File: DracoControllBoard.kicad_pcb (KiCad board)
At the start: 2 copper layers, 96.5 x 61.5 mm, 22 parts, among them SW1 SW_Push, SW10 SW_Push, SW11 SW_Push, SW12 SW_Push, SW2 SW_Push, SW3 SW_Push, SW4 SW_Push, SW5 SW_Push, SW6 SW_Push, SW7 SW_Push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

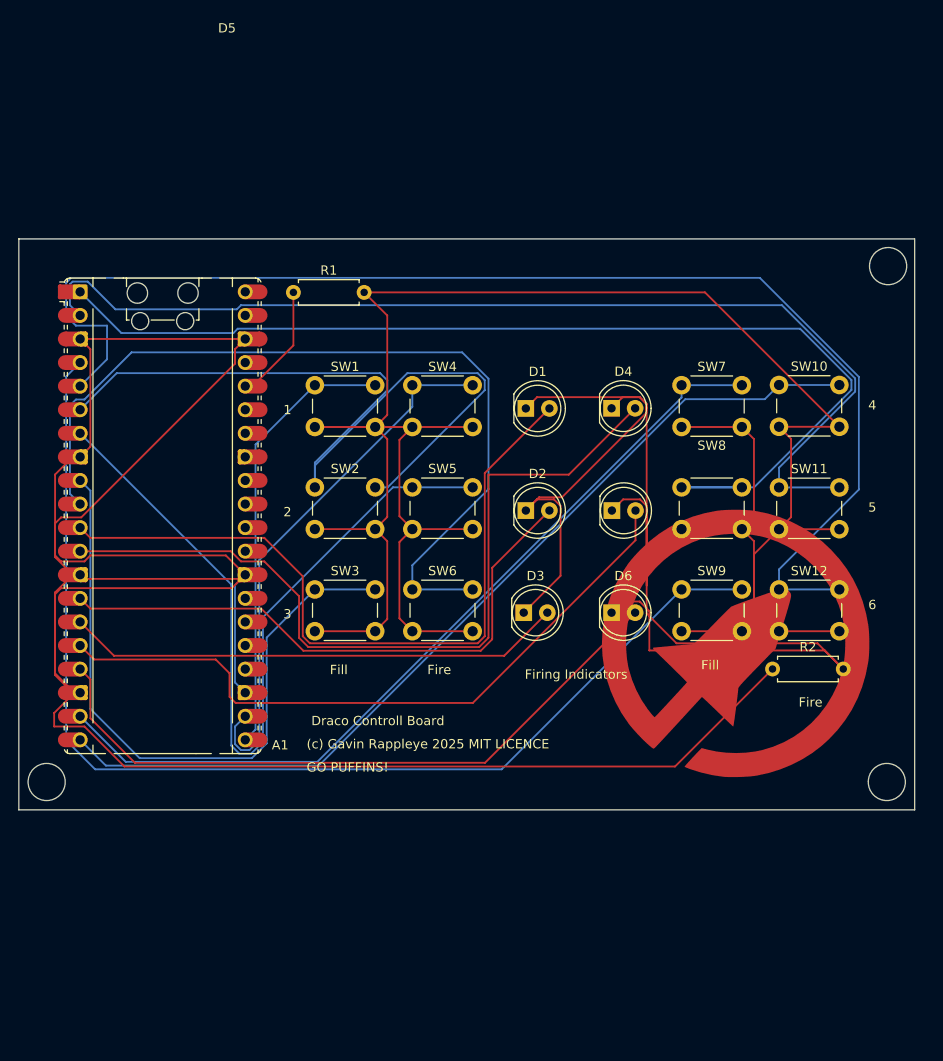
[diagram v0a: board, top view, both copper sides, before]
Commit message: fixted resistor issues
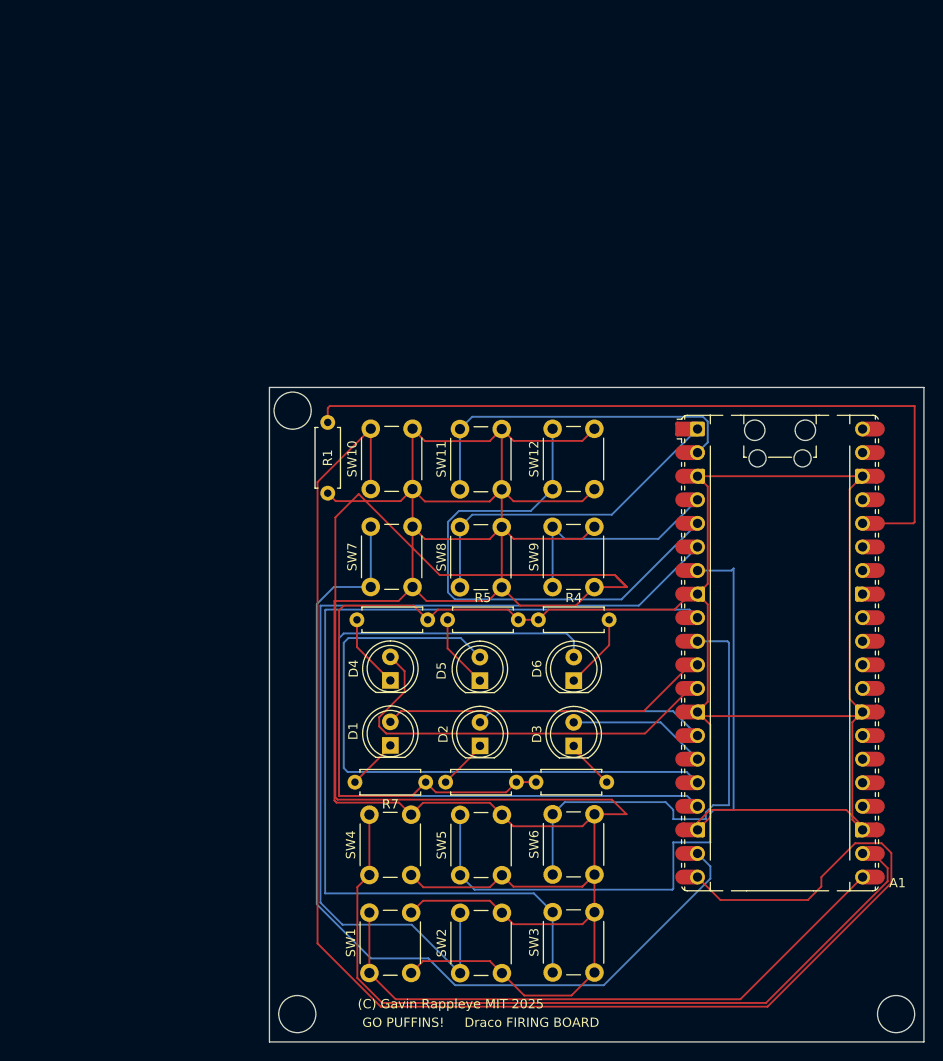
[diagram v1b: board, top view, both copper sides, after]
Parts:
- removed G***: LOGO, LOGO
- added R3: R, Resistor_THT:R_Axial_DIN0207_L6.3mm_D2.5mm_P7.62mm_Horizontal, F.Cu at (54.5, 67.0)
- added R4: R, Resistor_THT:R_Axial_DIN0207_L6.3mm_D2.5mm_P7.62mm_Horizontal, F.Cu at (64.5, 49.5)
- added R5: R, Resistor_THT:R_Axial_DIN0207_L6.3mm_D2.5mm_P7.62mm_Horizontal, F.Cu at (54.7, 49.5)
- added R6: R, Resistor_THT:R_Axial_DIN0207_L6.3mm_D2.5mm_P7.62mm_Horizontal, F.Cu at (52.5, 49.5)
- added R7: R, Resistor_THT:R_Axial_DIN0207_L6.3mm_D2.5mm_P7.62mm_Horizontal, F.Cu at (52.3, 67.0)
- moved A1 68.1 mm to (90.5, 53.1)
- moved SW1 63.6 mm to (46.3, 87.6), turned to 90 degrees
- moved SW2 54.6 mm to (56.0, 87.6), turned to 90 degrees
- moved SW4 53.0 mm to (46.3, 77.0), turned to 90 degrees
- moved SW3 48.6 mm to (66.0, 87.5), turned to 90 degrees
- moved SW10 45.4 mm to (46.4, 35.4), turned to 90 degrees
- moved SW5 42.1 mm to (56.0, 77.0), turned to 90 degrees
- moved SW7 39.9 mm to (46.4, 46.0), turned to 90 degrees
- moved D1 39.1 mm to (48.5, 63.1), turned to 90 degrees
- moved D4 37.8 mm to (48.5, 56.1), turned to 90 degrees
- moved SW11 34.4 mm to (56.0, 35.5), turned to 90 degrees
- moved SW6 34.2 mm to (66.0, 77.0), turned to 90 degrees
- moved R2 28.2 mm to (64.2, 67.0)
- moved SW12 26.7 mm to (66.0, 35.5), turned to 90 degrees
- moved SW8 26.2 mm to (56.0, 46.0), turned to 90 degrees
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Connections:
- D2 pad 1: Net-(D1-K) -> Net-(D2-K)
- D3 pad 1: Net-(D1-K) -> Net-(D3-K)
- D4 pad 1: Net-(D1-K) -> Net-(D4-K)
- D5 pad 1: Net-(D1-K) -> Net-(D5-K)
- D6 pad 1: Net-(D1-K) -> Net-(D6-K)
- R2 pad 2: Net-(D1-K) -> Net-(D3-K)
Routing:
- net Net-(D1-K): track 150.6 -> 5.54 mm
- net Net-(R1-Pad2): track 263.7 -> 387.5 mm
- net Net-(A1-GPIO2): track 123.4 -> 24.4 mm
- net Net-(A1-GPIO3): track 139.1 -> 57.4 mm
- net Net-(A1-GPIO0): track 117.6 -> 36.5 mm
- net Net-(A1-GPIO1): track 114.8 -> 37.8 mm
- net Net-(A1-3V3): track 12.7 -> 83.0 mm
- net Net-(A1-GPIO15): track 99.9 -> 163.2 mm
- net Net-(A1-GND-Pad13): track 271.4 -> 222.5 mm
- net Net-(A1-GPIO8): track 80.3 -> 34.8 mm
- net Net-(A1-GPIO7): track 92.3 -> 49.4 mm
- net Net-(A1-GPIO9): track 87.6 -> 45.1 mm
- net Net-(A1-GPIO11): track 53.8 -> 15.0 mm
- net Net-(A1-GPIO10): track 63.7 -> 25.0 mm
- net Net-(A1-GPIO6): track 72.1 -> 102.8 mm
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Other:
- board size 96.5 x 61.5 mm -> 70.5 x 70.5 mm
- board text added: "(C) Gavin Rappleye MIT 2025"
- board text added: "Draco FIRING BOARD"
- board text removed: "(c) Gavin Rappleye 2025 MIT LICENCE"
- board text removed: "1"
- board text removed: "2"
- board text removed: "3"
- board text removed: "4"
- board text removed: "5"
- board text removed: "6"
- board text removed: "Draco Controll Board"
- board text removed: "Fill"
- board text removed: "Fire"
- board text removed: "Firing Indicators"

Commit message: fixed resistor issue
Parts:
- added G***: LOGO, LOGO, F.Cu at (94.5, 88.0)
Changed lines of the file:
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@@
 		)
+	)
+	(footprint "LOGO"
+		(layer "F.Cu")
+		(at 94.5 88)
+		(property "Reference" "G***"
+			(at 0 0 0)
+			(layer "F.SilkS")
+			(hide yes)
+			(effects
+				(font
+					(size 1.5 1.5)
+					(thickness 0.3)
+				)
+			)
+		)
+		(property "Value" "LOGO"
+			(at 0.75 0 0)
+			(layer "F.SilkS")
+			(hide yes)
+			(effects
+				(font
+					(size 1.5 1.5)
+					(thickness 0.3)
+				)
+			)
+		)
+		(property "Datasheet" ""
+			(at 0 0 0)
+			(layer "F.Fab")
+			(hide yes)
+			(effects
+				(font
+					(size 1.27 1.27)
+					(thickness 0.15)
+				)
+			)
+		)
+		(property "Description" ""
+			(at 0 0 0)
+			(layer "F.Fab")
+			(hide yes)
+			(effects
+				(font
+					(size 1.27 1.27)
+					(thickness 0.15)
+				)
+			)
+		)
+		(attr board_only exclude_from_pos_files exclude_from_bom)
+		(fp_poly
+			(pts
+				(xy 0.118143 -5.388697) (xy 0.357 -5.381528) (xy 0.575854 -5.36721) (xy 0.761255 -5.345751) (xy 0.768242 -5.344673)
+				(xy 1.278537 -5.241701) (xy 1.769139 -5.095643) (xy 2.238526 -4.907275) (xy 2.685177 -4.677372)
+				(xy 3.107571 -4.40671) (xy 3.504185 -4.096064) (xy 3.843367 -3.777288) (xy 4.184987 -3.397336) (xy 4.482661 -3.000877)
+				(xy 4.737578 -2.585505) (xy 4.950932 -2.14881) (xy 5.123916 -1.688386) (xy 5.25772 -1.201822) (xy 5.344915 -0.744235)
+				(xy 5.367057 -0.55422) (xy 5.381467 -0.330902) (xy 5.38814 -0.088365) (xy 5.387073 0.159305) (xy 5.37826 0.398021)
+				(xy 5.361697 0.6137) (xy 5.345367 0.744234) (xy 5.243642 1.259516) (xy 5.099213 1.753452) (xy 4.912631 2.225052)
+				(xy 4.684451 2.673324) (xy 4.415224 3.097277) (xy 4.105506 3.49592) (xy 3.755848 3.868262) (xy 3.445085 4.14876)
+				(xy 3.076103 4.428857) (xy 2.673871 4.679612) (xy 2.245363 4.897905) (xy 1.797552 5.080616) (xy 1.337412 5.224624)
+				(xy 0.871914 5.326809) (xy 0.77833 5.342023) (xy 0.639332 5.358652) (xy 0.466882 5.372217) (xy 0.27364 5.382367)
+				(xy 0.072265 5.388752) (xy -0.124584 5.391024) (xy -0.304247 5.388831) (xy -0.454066 5.381825) (xy -0.504159 5.377456)
+				(xy -0.956599 5.309708) (xy -1.418939 5.20063) (xy -1.818573 5.074906) (xy -1.918247 5.038308) (xy -1.998539 5.005898)
+				(xy -2.050182 4.981609) (xy -2.06465 4.970505) (xy -2.04907 4.948244) (xy -2.006096 4.89735) (xy -1.941381 4.824023)
+				(xy -1.86058 4.734465) (xy -1.769343 4.634875) (xy -1.673325 4.531456) (xy -1.578177 4.430408) (xy -1.489554 4.337931)
+				(xy -1.464717 4.312411) (xy -1.373833 4.219435) (xy -1.137058 4.281677) (xy -0.769393 4.35898) (xy -0.380285 4.405279)
+				(xy 0.018233 4.42049) (xy 0.414132 4.404531) (xy 0.795379 4.357321) (xy 1.082212 4.296875) (xy 1.525297 4.159592)
+				(xy 1.946316 3.980268) (xy 2.343161 3.760392) (xy 2.713729 3.501453) (xy 3.055912 3.204938) (xy 3.367606 2.872337)
+				(xy 3.646704 2.505137) (xy 3.673521 2.465401) (xy 3.908408 2.075462) (xy 4.098174 1.675672) (xy 4.245603 1.259472)
+				(xy 4.336723 0.901952) (xy 4.370103 0.705246) (xy 4.394861 0.475535) (xy 4.410586 0.226707) (xy 4.416867 -0.027353)
+				(xy 4.413293 -0.272756) (xy 4.399454 -0.495614) (xy 4.382295 -0.638287) (xy 4.288011 -1.102084)
+				(xy 4.151752 -1.542576) (xy 3.973468 -1.959865) (xy 3.753107 -2.354053) (xy 3.490617 -2.725244)
+				(xy 3.185947 -3.073538) (xy 3.129697 -3.130736) (xy 2.806722 -3.422834) (xy 2.45534 -3.683432) (xy 2.0818 -3.909045)
+				(xy 1.692352 -4.096193) (xy 1.293245 -4.241391) (xy 0.996314 -4.319575) (xy 0.640375 -4.380476)
+				(xy 0.264732 -4.412798) (xy -0.119473 -4.416973) (xy -0.501096 -4.393437) (xy -0.868994 -4.342623)
+				(xy -1.212024 -4.264965) (xy -1.33242 -4.228867) (xy -1.76712 -4.064169) (xy -2.176785 -3.859708)
+				(xy -2.559332 -3.617692) (xy -2.912681 -3.340329) (xy -3.234752 -3.029827) (xy -3.523463 -2.688393)
+				(xy -3.776735 -2.318235) (xy -3.992486 -1.921561) (xy -4.168636 -1.500579) (xy -4.296484 -1.083748)
+				(xy -4.360027 -0.772425) (xy -4.400687 -0.434195) (xy -4.418398 -0.081863) (xy -4.413095 0.271767)
+				(xy -4.384714 0.613892) (xy -4.333189 0.931706) (xy -4.307304 1.044329) (xy -4.176117 1.474275)
+				(xy -4.003662 1.889783) (xy -3.793281 2.284272) (xy -3.548319 2.651156) (xy -3.389185 2.851698)
+				(xy -3.333559 2.913841) (xy -3.289172 2.956871) (xy -3.265271 2.971865) (xy -3.264822 2.971736)
+				(xy -3.244452 2.952886) (xy -3.196186 2.903408) (xy -3.124287 2.827915) (xy -3.033018 2.731017)
+				(xy -2.92664 2.617326) (xy -2.809415 2.491453) (xy -2.685607 2.35801) (xy -2.559477 2.221606) (xy -2.435287 2.086855)
+				(xy -2.3173 1.958366) (xy -2.209778 1.840752) (xy -2.116983 1.738622) (xy -2.043177 1.65659) (xy -1.992623 1.599265)
+				(xy -1.969582 1.571259) (xy -1.96862 1.569401) (xy -1.985107 1.549871) (xy -2.031525 1.501424) (xy -2.10331 1.428545)
+				(xy -2.195898 1.335717) (xy -2.304727 1.227424) (xy -2.425232 1.10815) (xy -2.552851 0.982379) (xy -2.683018 0.854594)
+				(xy -2.811171 0.729279) (xy -2.932746 0.610918) (xy -3.04318 0.503996) (xy -3.137908 0.412994) (xy -3.212368 0.342399)
+				(xy -3.261995 0.296692) (xy -3.277383 0.283525) (xy -3.320987 0.237272) (xy -3.336201 0.19582) (xy -3.320361 0.170832)
+				(xy -3.303774 0.168053) (xy -3.272424 0.165838) (xy -3.199321 0.159561) (xy -3.090505 0.149776)
+				(xy -2.952017 0.137035) (xy -2.789896 0.121892) (xy -2.610182 0.104899) (xy -2.517526 0.096064)
+				(xy -2.330549 0.078328) (xy -2.157446 0.062175) (xy -2.004413 0.048162) (xy -1.877642 0.036847)
+				(xy -1.783327 0.028786) (xy -1.727663 0.024537) (xy -1.716541 0.024015) (xy -1.686061 0.006393)
+				(xy -1.623847 -0.046) (xy -1.530577 -0.13251) (xy -1.40693 -0.252486) (xy -1.253584 -0.405273) (xy -1.071218 -0.590219)
+				(xy -0.96187 -0.702248) (xy -0.80855 -0.85926) (xy -0.663187 -1.007076) (xy -0.529702 -1.141783)
+				(xy -0.41202 -1.259468) (xy -0.314064 -1.356217) (xy -0.239758 -1.428116) (xy -0.193025 -1.471252)
+				(xy -0.181624 -1.480532) (xy -0.143633 -1.499418) (xy -0.065359 -1.531951) (xy 0.048058 -1.576208)
+				(xy 0.191479 -1.630265) (xy 0.359766 -1.692199) (xy 0.547779 -1.760087) (xy 0.750382 -1.832005)
+				(xy 0.86065 -1.870655) (xy 1.116048 -1.959607) (xy 1.330356 -2.033429) (xy 1.507779 -2.092926) (xy 1.65252 -2.138904)
+				(xy 1.768783 -2.172167) (xy 1.860772 -2.19352) (xy 1.932692 -2.203768) (xy 1.988746 -2.203716) (xy 2.033138 -2.194168)
+				(xy 2.070073 -2.175929) (xy 2.103755 -2.149805) (xy 2.138387 -2.1166) (xy 2.139497 -2.11549) (xy 2.195909 -2.053081)
+				(xy 2.223768 -2.000148) (xy 2.232437 -1.936707) (xy 2.232703 -1.916531) (xy 2.227953 -1.87397) (xy 2.213313 -1.803327)
+				(xy 2.1882 -1.702591) (xy 2.152031 -1.56975) (xy 2.104222 -1.402795) (xy 2.044189 -1.199714) (xy 1.971351 -0.958496)
+				(xy 1.885121 -0.677131) (xy 1.784919 -0.353606) (xy 1.703693 -0.093115) (xy 1.608989 0.209895) (xy 0.858511 0.97992)
+				(xy 0.677721 1.165749) (xy 0.527888 1.32066) (xy 0.406176 1.447844) (xy 0.309748 1.550491) (xy 0.235767 1.631792)
+				(xy 0.181396 1.694937) (xy 0.143799 1.743116) (xy 0.120138 1.779521) (xy 0.107577 1.807341) (xy 0.103307 1.829273)
+				(xy 0.097405 1.900655) (xy 0.086602 2.004505) (xy 0.071793 2.134058) (xy 0.053876 2.282549) (xy 0.033745 2.443211)
+				(xy 0.012298 2.609281) (xy -0.009569 2.773992) (xy -0.03096 2.930579) (xy -0.050979 3.072277) (xy -0.06873 3.19232)
+				(xy -0.083315 3.283943) (xy -0.093839 3.340381) (xy -0.098908 3.355641) (xy -0.120103 3.337908)
+				(xy -0.171406 3.290805) (xy -0.248494 3.218426) (xy -0.347042 3.124868) (xy -0.462727 3.014223)
+				(xy -0.591225 2.890588) (xy -0.652835 2.831072) (xy -0.78984 2.698818) (xy -0.919619 2.574027) (xy -1.037094 2.461545)
+				(xy -1.137185 2.36622) (xy -1.214813 2.292898) (xy -1.264899 2.246426) (xy -1.275222 2.23719) (xy -1.36207 2.161292)
+				(xy -1.995449 2.84994) (xy -2.232703 3.107823) (xy -2.439588 3.332511) (xy -2.618171 3.526212) (xy -2.770522 3.691132)
+				(xy -2.898707 3.829477) (xy -3.004796 3.943454) (xy -3.090856 4.03527) (xy -3.158956 4.107132) (xy -3.211163 4.161247)
+				(xy -3.249546 4.199821) (xy -3.276173 4.225061) (xy -3.293112 4.239174) (xy -3.302252 4.244322)
+				(xy -3.338305 4.232515) (xy -3.400882 4.189309) (xy -3.485072 4.119598) (xy -3.585964 4.028278)
+				(xy -3.698648 3.920243) (xy -3.818211 3.80039) (xy -3.939745 3.673613) (xy -4.058337 3.544807) (xy -4.169077 3.418868)
+				(xy -4.267054 3.30069) (xy -4.327646 3.222202) (xy -4.609836 2.80273) (xy -4.848738 2.365456) (xy -5.044371 1.913318)
+				(xy -5.196751 1.449254) (xy -5.305896 0.976203) (xy -5.371824 0.497103) (xy -5.394552 0.014892)
+				(xy -5.374098 -0.467492) (xy -5.310479 -0.947111) (xy -5.203712 -1.421027) (xy -5.053816 -1.886301)
+				(xy -4.860807 -2.339996) (xy -4.624703 -2.779173) (xy -4.345522 -3.200894) (xy -4.288951 -3.277032)
+				(xy -4.220279 -3.362415) (xy -4.127412 -3.470281) (xy -4.020344 -3.589401) (xy -3.90907 -3.708547)
+				(xy -3.854816 -3.764788) (xy -3.477453 -4.118183) (xy -3.077083 -4.42944) (xy -2.65388 -4.698471)
+				(xy -2.208018 -4.925185) (xy -1.739668 -5.109496) (xy -1.249004 -5.251313) (xy -0.768242 -5.345697)
+				(xy -0.583907 -5.367216) (xy -0.365762 -5.38155) (xy -0.127261 -5.388707)
+			)
+			(stroke
+				(width 0)
+				(type solid)
+			)
+			(fill yes)
+			(layer "F.SilkS")
+		)
+		(embedded_fonts no)
 	)
 	(footprint "Resistor_THT:R_Axial_DIN0207_L6.3mm_D2.5mm_P7.62mm_Horizontal"
